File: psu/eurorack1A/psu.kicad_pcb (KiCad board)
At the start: 2 copper layers, 245.1 x 30.5 mm, 37 parts, among them J1 Conn_01x02_Male, J10 Conn_02x08_Odd_Even, J11 Conn_02x08_Odd_Even, J12 Conn_02x08_Odd_Even, J13 Conn_02x08_Odd_Even, J2 Conn_01x02_Male, J3 Conn_01x02_Male, J4 Conn_02x08_Odd_Even, J5 Conn_02x08_Odd_Even, J6 Conn_02x08_Odd_Even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

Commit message: Preparations for next revision
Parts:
- removed SW1: SW_MEC_5G_LED, Connector_PinHeader_2.54mm:PinHeader_1x04_P2.54mm_Vertical
- added R4: R, Resistor_THT:R_Axial_DIN0207_L6.3mm_D2.5mm_P10.16mm_Horizontal, F.Cu at (55.9, 113.0)
- added R5: R, Resistor_THT:R_Axial_DIN0207_L6.3mm_D2.5mm_P10.16mm_Horizontal, F.Cu at (55.9, 117.1)
- added SW2: Conn_02x03_Odd_Even, Connector_PinHeader_2.54mm:PinHeader_2x03_P2.54mm_Vertical, F.Cu at (125.1, 130.2)
- moved D1 3.86 mm to (61.6, 95.2)
- moved R1 3.17 mm to (50.8, 83.2)
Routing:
- net VIN: track 9.94 -> 6.13 mm
- net Net-(D1-Pad1): track 8.45 -> 6.24 mm
- net Net-(J1-Pad1): track 49.4 -> 47.4 mm
- net +5V: track 249.4 -> 251.0 mm

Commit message: dropped option 1
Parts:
- removed C7, C8: 22u/50V, Capacitor_THT:CP_Radial_D6.3mm_P2.50mm
- removed D2, D3: 1N5406RLG, Diode_THT:D_DO-41_SOD81_P10.16mm_Horizontal
- removed R2, R3: 0R, Resistor_THT:R_Axial_DIN0207_L6.3mm_D2.5mm_P10.16mm_Horizontal
- removed U5: VR20S12, Package_TO_SOT_THT:TO-220-3_Vertical
- D1: footprint Diode_THT:D_DO-41_SOD81_P10.16mm_Horizontal -> Diode_THT:D_DO-201AD_P15.24mm_Horizontal
- moved SW2 79.9 mm to (49.9, 103.1)
- moved R5 31.6 mm to (49.9, 86.1), turned to 270 degrees
- moved R4 27.0 mm to (54.0, 86.1), turned to 270 degrees
- moved D1 7.19 mm to (60.9, 88.1), turned to 270 degrees
- moved J1 2.70 mm to (44.9, 99.1)
- moved J3 0.65 mm to (58.4, 78.1)
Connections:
- D1 pad 1: Net-(D1-Pad1) -> VIN
- D1 pad 2: VIN -> GND
- U1 pad 1: Net-(D1-Pad1) -> VIN
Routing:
- net Net-(J1-Pad1): track 47.4 -> 0.00 mm
- net Net-(C8-Pad1): track 38.6 -> 0.00 mm
- net Net-(C7-Pad1): track 31.4 -> 0.00 mm
- net Net-(R1-Pad2): track 12.8 -> 0.00 mm
- net Net-(D1-Pad1): track 6.24 -> 0.00 mm
- net VIN: track 6.13 -> 0.00 mm

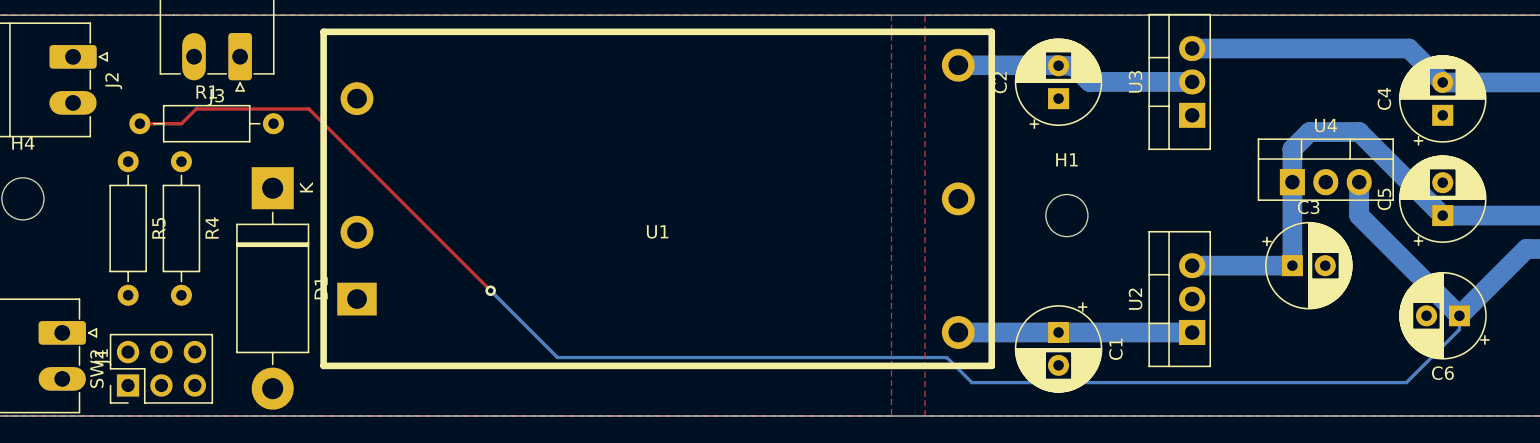
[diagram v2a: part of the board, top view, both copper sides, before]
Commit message: added DKMW30
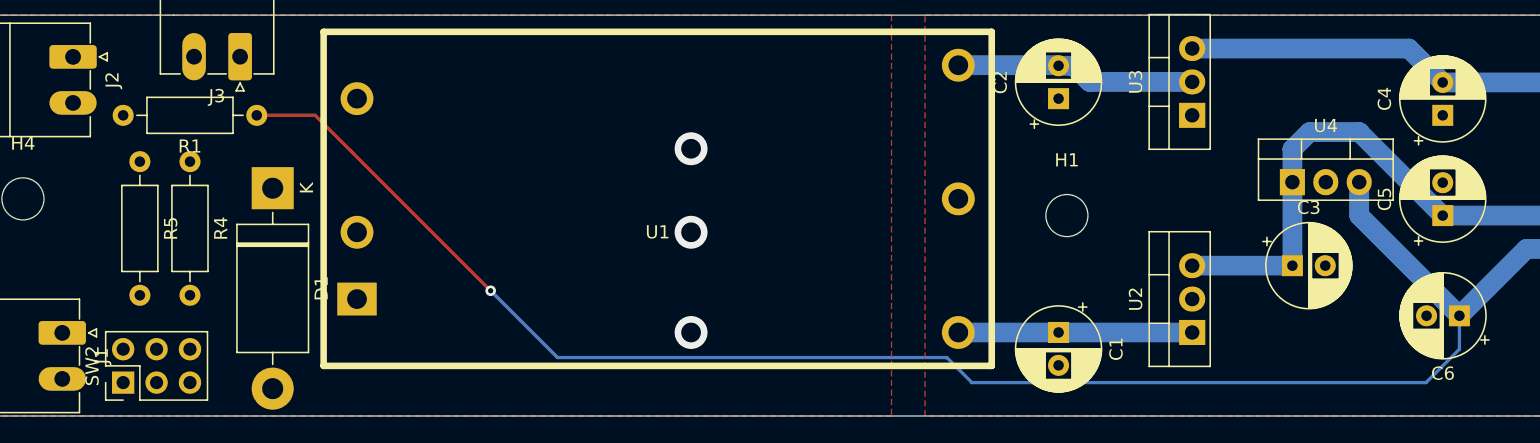
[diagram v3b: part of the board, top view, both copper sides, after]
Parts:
- moved R1 8.91 mm to (59.7, 82.5), turned to 180 degrees
- moved R5 0.89 mm to (50.8, 86.1)
- moved R4 0.65 mm to (54.6, 86.1)
- moved SW2 0.43 mm to (49.5, 102.9)
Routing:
- net +5V: track 251.0 -> 242.3 mm
- net VIN: vias 0 -> 1
- net GND: vias 0 -> 1
- net (no net): vias 0 -> 1
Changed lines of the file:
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@@
     (thickness 1.6)
     (drawings 6)
-    (tracks 42)
+    (tracks 44)
     (zones 0)
     (modules 32)
@@
   )
   (module Connector_PinHeader_2.54mm:PinHeader_2x03_P2.54mm_Vertical (layer F.Cu)
-    (at 49.9 103.09 90)
+    (at 49.53 102.87 90)
     (descr "Through hole straight pin header, 2x03, 2.54mm pitch, double rows")
     (tags "Through hole pin header THT 2x03 2.54mm double row")
@@
   )
   (module Resistor_THT:R_Axial_DIN0207_L6.3mm_D2.5mm_P10.16mm_Horizontal (layer F.Cu)
-    (at 49.91 86.07 270)
+    (at 50.8 86.07 270)
     (descr "Resistor, Axial_DIN0207 series, Axial, Horizontal, pin pitch=10.16mm, 0.25W = 1/4W, length*diameter=6.3*2.5mm^2, http://cdn-reichelt.de/documents/datenblatt/B400/1_4W%23YAG.pdf")
     (tags "Resistor Axial_DIN0207 series Axial Horizontal pin pitch 10.16mm 0.25W = 1/4W length 6.3mm diameter 2.5mm")
@@
   )
   (module Resistor_THT:R_Axial_DIN0207_L6.3mm_D2.5mm_P10.16mm_Horizontal (layer F.Cu)
-    (at 53.96 86.07 270)
+    (at 54.61 86.07 270)
     (descr "Resistor, Axial_DIN0207 series, Axial, Horizontal, pin pitch=10.16mm, 0.25W = 1/4W, length*diameter=6.3*2.5mm^2, http://cdn-reichelt.de/documents/datenblatt/B400/1_4W%23YAG.pdf")
     (tags "Resistor Axial_DIN0207 series Axial Horizontal pin pitch 10.16mm 0.25W = 1/4W length 6.3mm diameter 2.5mm")
@@
   )
   (module Resistor_THT:R_Axial_DIN0207_L6.3mm_D2.5mm_P10.16mm_Horizontal (layer F.Cu)
-    (at 50.8 83.185)
+    (at 59.69 82.55 180)
     (descr "Resistor, Axial_DIN0207 series, Axial, Horizontal, pin pitch=10.16mm, 0.25W = 1/4W, length*diameter=6.3*2.5mm^2, http://cdn-reichelt.de/documents/datenblatt/B400/1_4W%23YAG.pdf")
     (tags "Resistor Axial_DIN0207 series Axial Horizontal pin pitch 10.16mm 0.25W = 1/4W length 6.3mm diameter 2.5mm")
@@
       (effects (font (size 1 1) (thickness 0.15)))
     )
-    (pad 2 thru_hole oval (at 10.16 0) (size 1.6 1.6) (drill 0.8) (layers *.Cu *.Mask)
+    (pad 2 thru_hole oval (at 10.16 0 180) (size 1.6 1.6) (drill 0.8) (layers *.Cu *.Mask)
       (net 6 "Net-(R1-Pad2)"))
-    (pad 1 thru_hole circle (at 0 0) (size 1.6 1.6) (drill 0.8) (layers *.Cu *.Mask)
+    (pad 1 thru_hole circle (at 0 0 180) (size 1.6 1.6) (drill 0.8) (layers *.Cu *.Mask)
       (net 7 +5V))
     (model ${KISYS3DMOD}/Resistor_THT.3dshapes/R_Axial_DIN0207_L6.3mm_D2.5mm_P10.16mm_Horizontal.wrl
@@
   (segment (start 274.28 80.05) (end 274.32 80.01) (width 1.5) (layer B.Cu) (net 3))
   (segment (start 149.86 80.05) (end 274.28 80.05) (width 1.5) (layer B.Cu) (net 3))
+  (via (at 92.71 99.06) (size 2.5) (drill 1.5) (layers F.Cu B.Cu) (net 0))
+  (via (at 92.71 91.44) (size 2.5) (drill 1.5) (layers F.Cu B.Cu) (net 4))
+  (via (at 92.71 85.09) (size 2.5) (drill 1.5) (layers F.Cu B.Cu) (net 12))
   (segment (start 143.51 90.17) (end 151.13 97.79) (width 1.5) (layer B.Cu) (net 7))
   (segment (start 143.51 87.63) (end 143.51 90.17) (width 1.5) (layer B.Cu) (net 7))
@@
   (segment (start 151.13 97.79) (end 156.21 92.71) (width 1.5) (layer B.Cu) (net 7))
   (segment (start 158.75 92.71) (end 274.32 92.71) (width 1.5) (layer B.Cu) (net 7))
-  (segment (start 151.13 98.84) (end 147.1 102.87) (width 0.25) (layer B.Cu) (net 7))
-  (segment (start 151.13 97.79) (end 151.13 98.84) (width 0.25) (layer B.Cu) (net 7))
-  (segment (start 114.060002 102.87) (end 112.155002 100.965) (width 0.25) (layer B.Cu) (net 7))
-  (segment (start 147.1 102.87) (end 114.060002 102.87) (width 0.25) (layer B.Cu) (net 7))
   (via (at 77.47 95.885) (size 0.8) (drill 0.4) (layers F.Cu B.Cu) (net 7))
+  (segment (start 66.9925 85.4075) (end 66.819999 85.234999) (width 0.25) (layer F.Cu) (net 7))
+  (segment (start 77.47 95.885) (end 66.9925 85.4075) (width 0.25) (layer F.Cu) (net 7))
+  (segment (start 64.135 82.55) (end 64.4525 82.8675) (width 0.25) (layer F.Cu) (net 7))
+  (segment (start 59.69 82.55) (end 64.135 82.55) (width 0.25) (layer F.Cu) (net 7))
+  (segment (start 64.4525 82.8675) (end 66.9925 85.4075) (width 0.25) (layer F.Cu) (net 7))
   (segment (start 82.55 100.965) (end 77.47 95.885) (width 0.25) (layer B.Cu) (net 7))
   (segment (start 112.155002 100.965) (end 82.55 100.965) (width 0.25) (layer B.Cu) (net 7))
-  (segment (start 50.8 83.185) (end 53.975 83.185) (width 0.25) (layer F.Cu) (net 7))
-  (segment (start 55.100001 82.059999) (end 63.644999 82.059999) (width 0.25) (layer F.Cu) (net 7))
-  (segment (start 53.975 83.185) (end 55.100001 82.059999) (width 0.25) (layer F.Cu) (net 7))
-  (segment (start 63.644999 82.059999) (end 66.9925 85.4075) (width 0.25) (layer F.Cu) (net 7))
-  (segment (start 66.9925 85.4075) (end 66.819999 85.234999) (width 0.25) (layer F.Cu) (net 7))
-  (segment (start 77.47 95.885) (end 66.9925 85.4075) (width 0.25) (layer F.Cu) (net 7))
+  (segment (start 114.060002 102.87) (end 112.155002 100.965) (width 0.25) (layer B.Cu) (net 7))
+  (segment (start 148.59 102.87) (end 114.060002 102.87) (width 0.25) (layer B.Cu) (net 7))
+  (segment (start 151.13 97.79) (end 151.13 100.33) (width 0.25) (layer B.Cu) (net 7))
+  (segment (start 151.13 100.33) (end 148.59 102.87) (width 0.25) (layer B.Cu) (net 7))
   (segment (start 158.75 97.79) (end 274.32 97.79) (width 1.5) (layer B.Cu) (net 8))
   (segment (start 274.32 95.25) (end 158.75 95.25) (width 1.5) (layer B.Cu) (net 9))
